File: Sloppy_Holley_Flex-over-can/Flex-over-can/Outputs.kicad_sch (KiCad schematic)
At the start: 20 parts, among them U4 BTS3256D, U5 BTS3256D, U6 BTS3256D, U7 BTS3256D

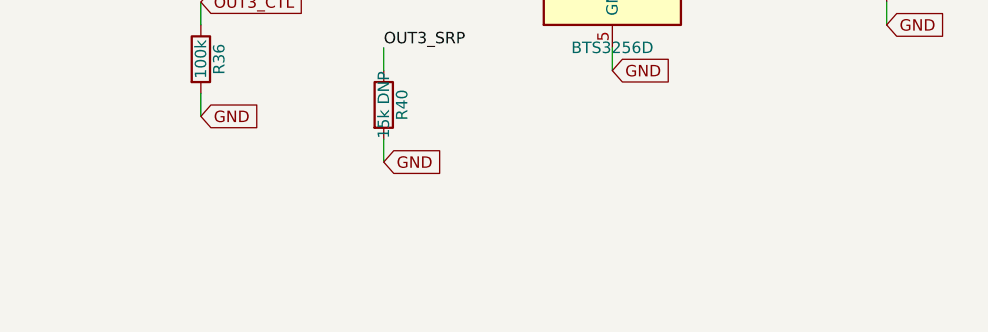
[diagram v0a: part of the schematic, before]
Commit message: Add PCB placement notes for decoupling caps to each sheet
Co-Authored-By: Claude Opus 5.5 <noreply@anthropic.com>
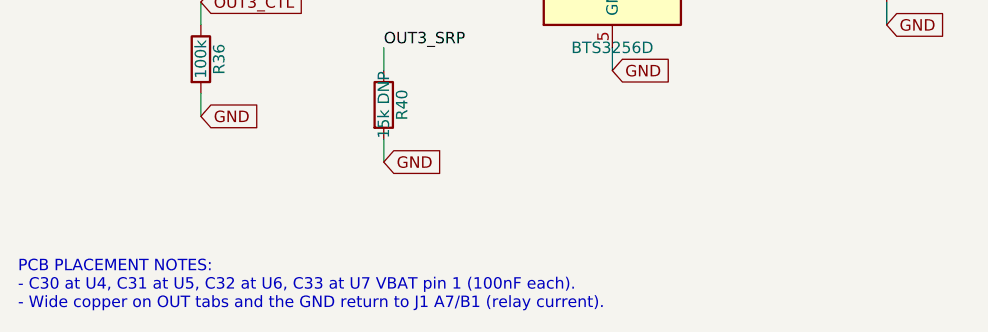
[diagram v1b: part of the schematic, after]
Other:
- note added: "PCB PLACEMENT NOTES: - C30 at U4, C31 at U5, C32 at U6, C33 at U7 VBAT pin 1 (100nF each). - Wide copper on OUT tabs and the GND return to J1 A7/B1 (relay current)."
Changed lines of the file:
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@@
 		)
 	)
+  (text "PCB PLACEMENT NOTES:\n- C30 at U4, C31 at U5, C32 at U6, C33 at U7 VBAT pin 1 (100nF each).\n- Wide copper on OUT tabs and the GND return to J1 A7/B1 (relay current)."
+    (at 15.24 180.34 0)
+    (effects (font (size 1.27 1.27) (color 0 0 194 1)) (justify left bottom))
+  )
 	(symbol
 		(lib_id "Device:R")
